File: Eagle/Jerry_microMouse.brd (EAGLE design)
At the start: 80 x 100 mm, 61 parts, among them IC1 DSPIC33FJ64MC804-PT, IC2 L293D, IC3 LM340MP-5.0, IC4 LM3940IMP-3.3

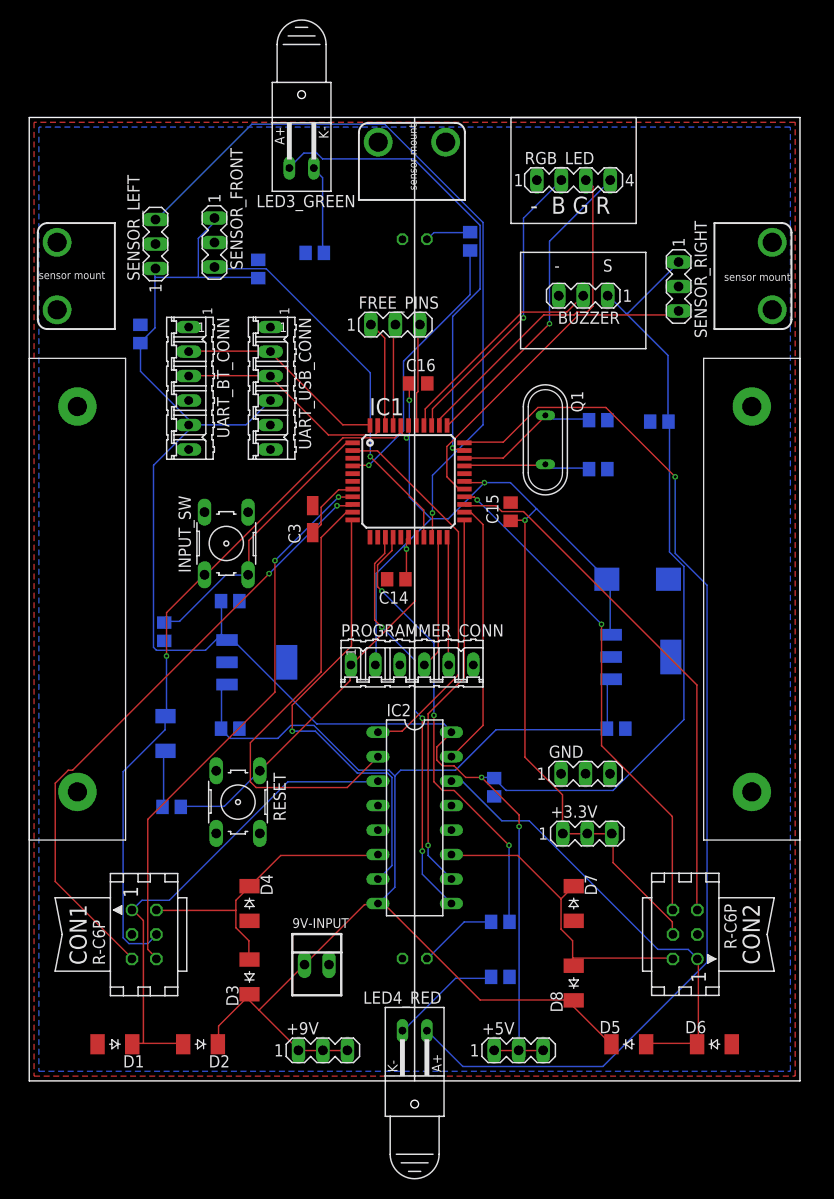
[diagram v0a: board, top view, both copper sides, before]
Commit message: update PCB, manually routing
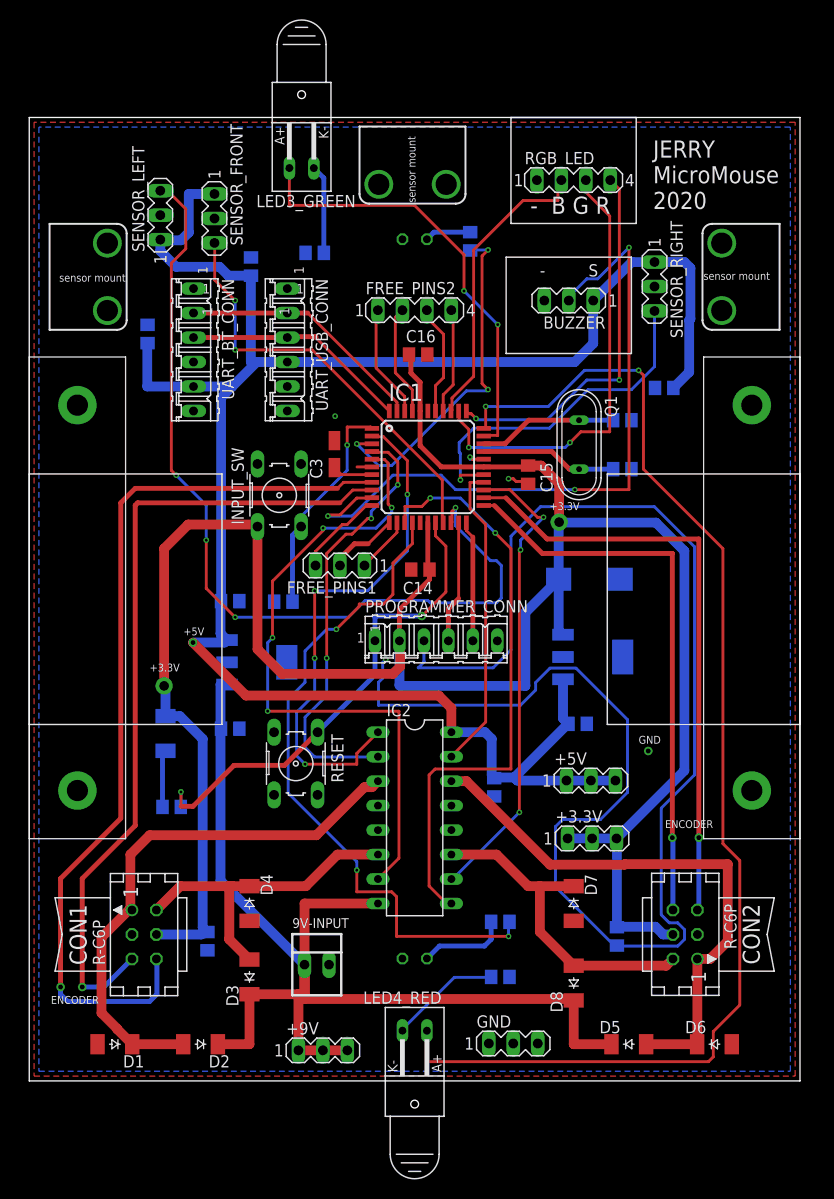
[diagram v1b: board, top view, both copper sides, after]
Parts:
- removed FREE_PINS: (no value), con-lstb:MA03-1
- added C13, C9: 100nF, rcl:C0805
- added FREE_PINS1: (no value), con-lstb:MA03-1
- added FREE_PINS2: (no value), con-lstb:MA04-1
- moved +5V 29.0 mm to (58.3, 31.2)
- moved GND 29.0 mm to (50.2, 3.88)
- moved U$1 25.5 mm to (5.00, 50.0)
- moved U$2 25.5 mm to (75.0, 50.0)
- moved SENS_MNT_L 13.3 mm to (34.3, 99.1), turned to 270 degrees
- moved SENS_MNT_R 13.0 mm to (2.11, 78.0), turned to 0 degrees
- moved SENS_MNT_F 12.8 mm to (77.9, 89.0), turned to 180 degrees
- moved R3 12.8 mm to (26.4, 49.7), turned to 180 degrees
- moved INPUT_SW 7.43 mm to (26.0, 60.8)
- moved RESET 7.21 mm to (27.7, 32.9)
- moved C3 7.12 mm to (31.7, 65.1)
- moved C7 5.00 mm to (58.1, 52.1)
- moved IC4 5.00 mm to (58.5, 44.0)
- moved UART_USB_CONN 4.37 mm to (26.8, 75.9)
- moved C15 4.25 mm to (51.8, 62.9), turned to 270 degrees
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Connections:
- net N$2 renamed RM_M+
- net N$4 renamed LM_M+
- net N$6 renamed RM_M-
- net N$7 renamed LM_M-
- new net BUZZER: BUZZER.2, IC1.10
- new net N$26: FREE_PINS2.4, IC1.37
- new net N$27: FREE_PINS1.2, IC1.12
- new net N$28: FREE_PINS1.1, IC1.13
- net +5V: now also C12.2, IC4.1
- net +9V: no longer C12.2, IC4.1
- net GND: now also C13.2, C9.2
- net LM_H_BRDG_DIR_1: now also IC1.4; no longer IC1.10
- net LM_H_BRDG_DIR_2: now also IC1.5; no longer IC1.11
- net N$1: now also IC1.3; no longer IC1.4
- net N$21: now also FREE_PINS1.3, IC1.11; no longer BUZZER.2, IC1.37
- net N$22: now also FREE_PINS2.1; no longer FREE_PINS.1
- net N$23: now also FREE_PINS2.2; no longer FREE_PINS.2
- net N$24: now also FREE_PINS2.3; no longer FREE_PINS.3
- net RM_ENC_CH_A: now also IC1.23; no longer IC1.26
- net RM_ENC_CH_B: now also IC1.24; no longer IC1.25
- net RM_H_BRDG_DIR_1: now also IC1.26; no longer IC1.24
- net RM_H_BRDG_DIR_2: now also IC1.25; no longer IC1.23
- net UART2_RX: now also IC1.44; no longer IC1.43
- net UART2_TX: now also IC1.43; no longer IC1.44
- net VDD: now also C13.1, C9.1
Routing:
- net GND: track 0.00 -> 171.6 mm, vias 0 -> 5
- net BUZZER: track 0.00 -> 72.9 mm, vias 0 -> 3
- net VDD: track 199.5 -> 243.8 mm, vias 6 -> 2
- net LM_ENC_CH_A: track 58.0 -> 94.8 mm, vias 2 -> 1
- net N$14: track 47.0 -> 70.3 mm
- net +5V: track 234.6 -> 211.4 mm, vias 2 -> 1
- net +9V: track 137.0 -> 116.0 mm
- net LM_H_BRDG_DIR_2: track 48.1 -> 68.3 mm, vias 1 -> 4
- net PWM_1_RIGHT_MOTOR: track 41.8 -> 61.5 mm, vias 3 -> 2
- net LM_ENC_CH_B: track 64.4 -> 83.9 mm, vias 2 -> 1
- net N$15: track 113.2 -> 129.6 mm, vias 1 -> 2
- net ADC_CH_2: track 77.2 -> 91.4 mm, vias 1 -> 4
- net PWM_2_LEFT_MOTOR: track 40.1 -> 54.2 mm, vias 0 -> 4
- net N$21: track 23.1 -> 9.31 mm
- net N$18: track 34.9 -> 46.7 mm, vias 0 -> 2
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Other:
- board text added: "+3.3V"
- board text added: "+5V"
- board text added: "ENCODER"
- board text added: "GND"
- board text added: "JERRY MicroMouse 2020"
